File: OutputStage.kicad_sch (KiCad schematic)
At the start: 13 parts, among them SW10 SW_DPDT_x2, SW11 SW_Rotary_1x7, U5 BUF634A

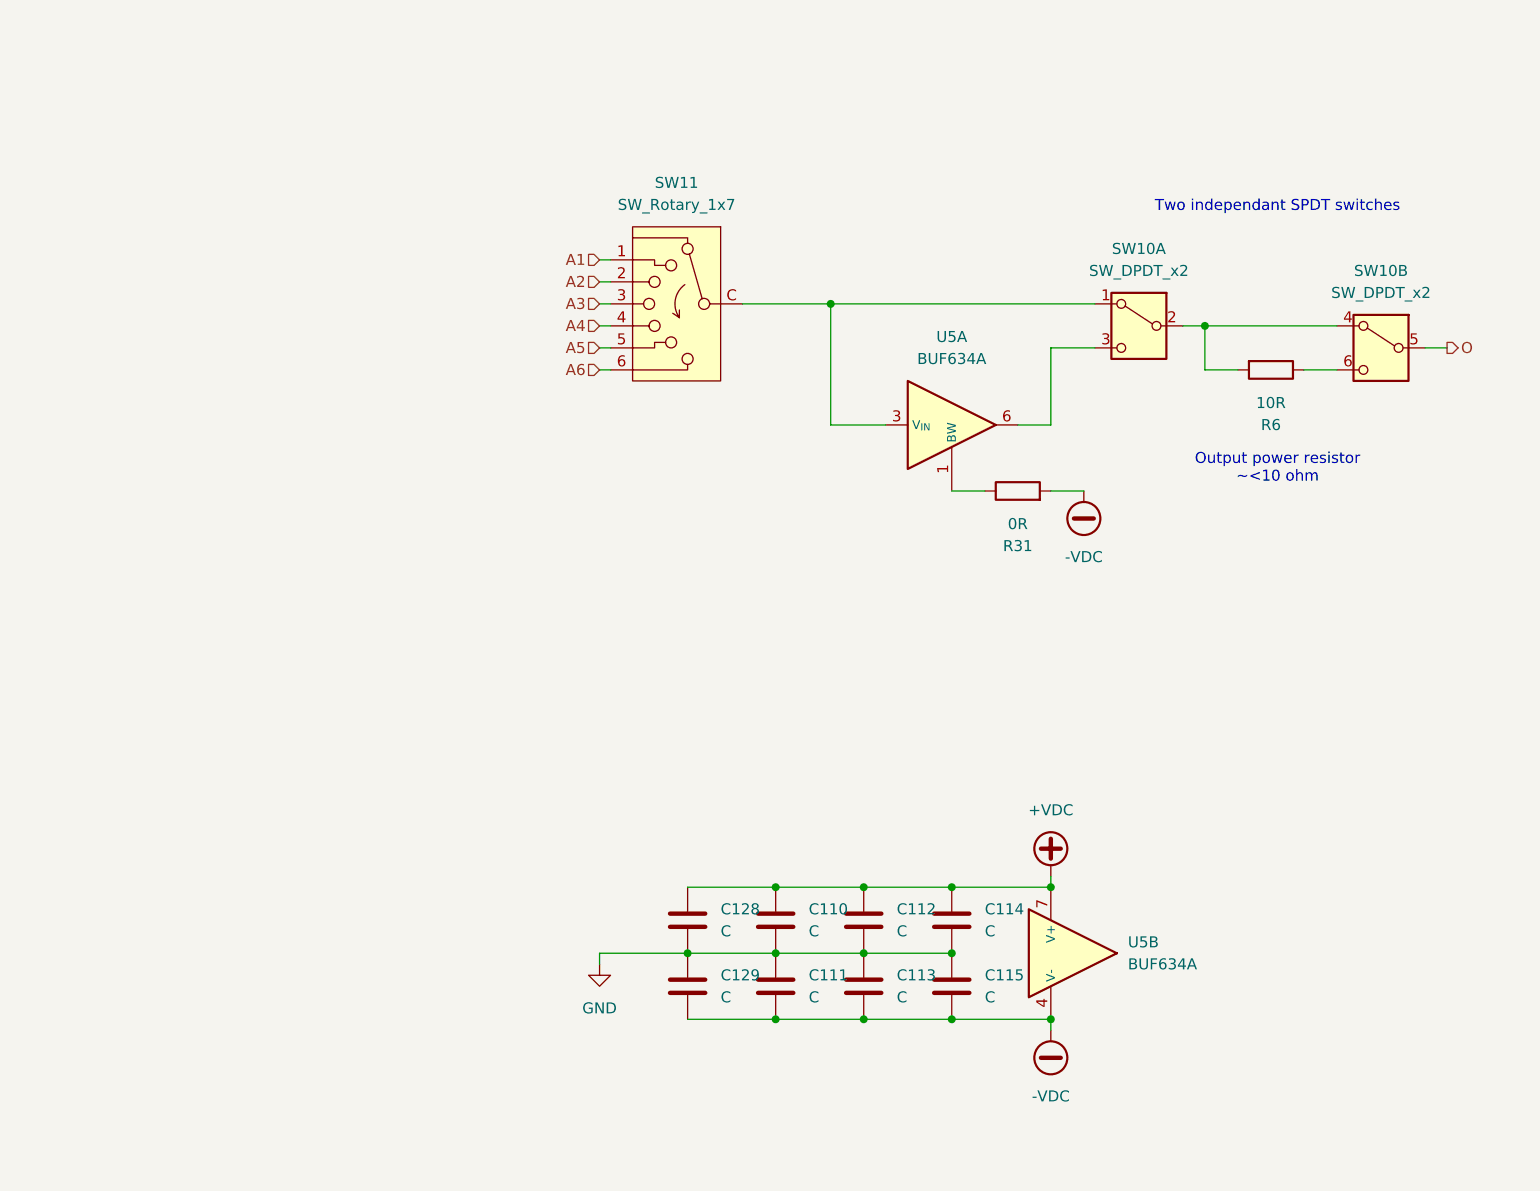
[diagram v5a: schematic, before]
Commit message: Voltage controlled current output circuit and preliminary layout added
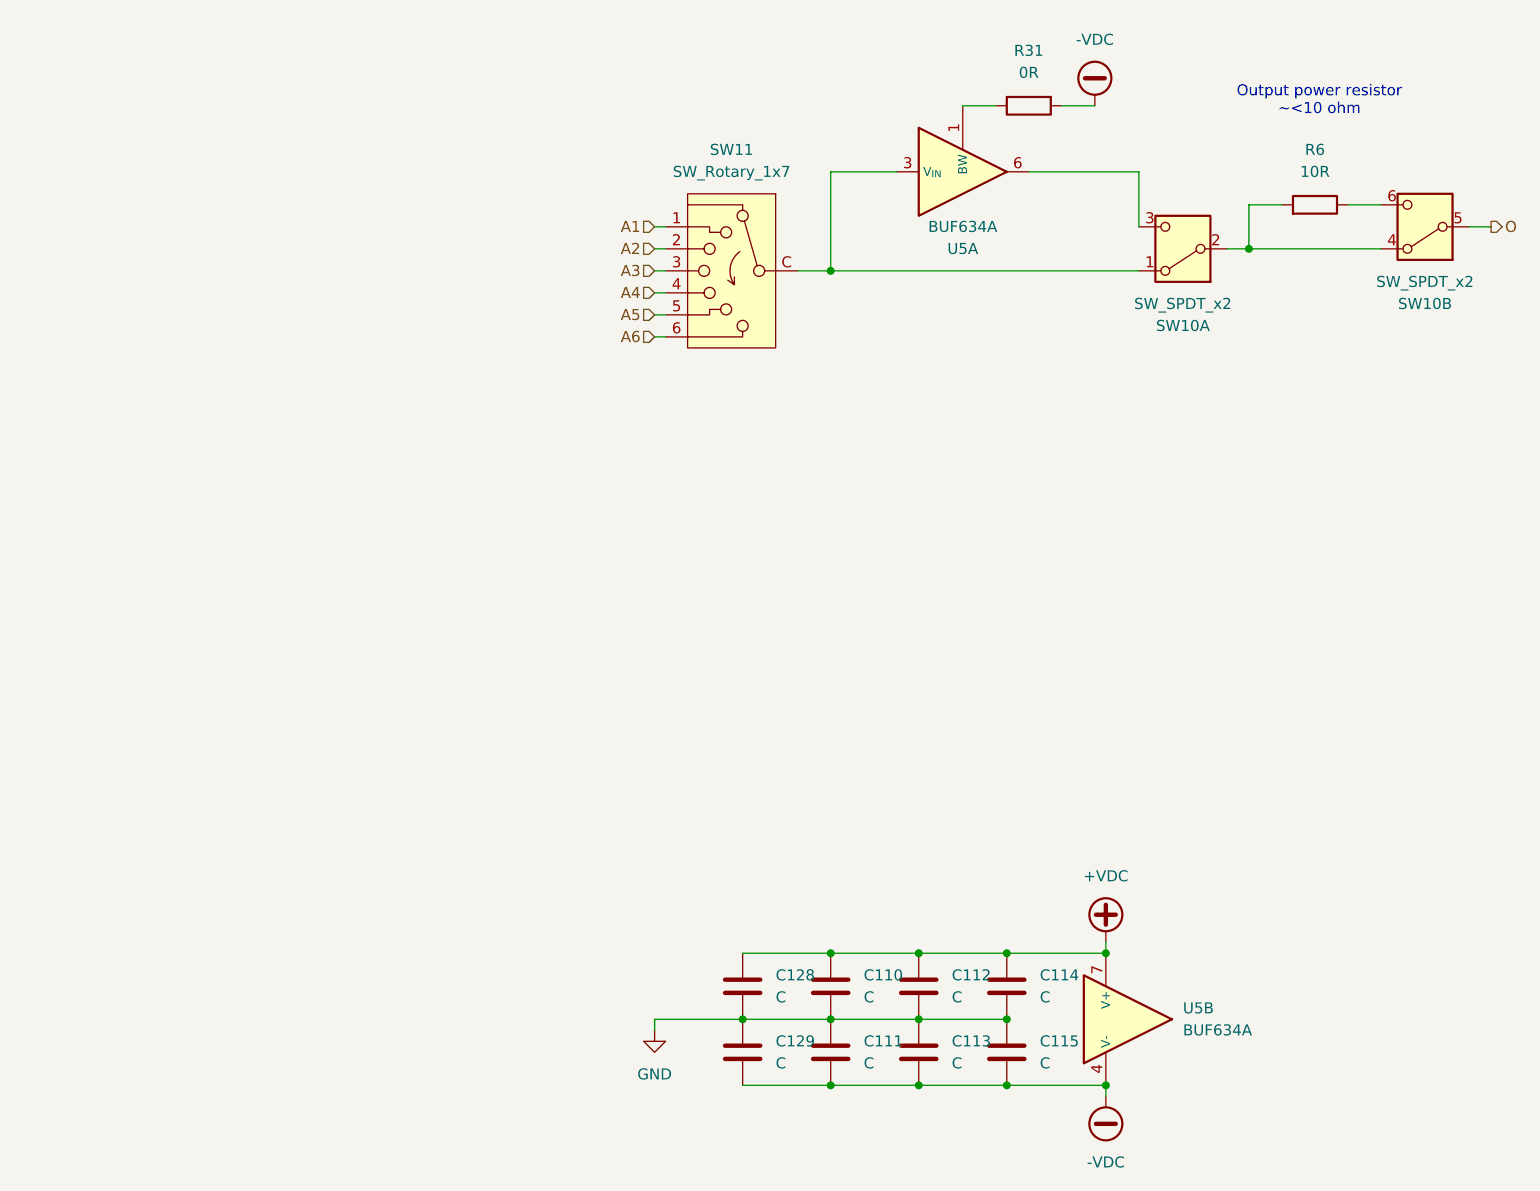
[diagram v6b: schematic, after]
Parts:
- SW10: value SW_DPDT_x2 -> SW_SPDT_x2
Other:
- note removed: "Two independant SPDT switches"
- moved on the sheet: C110, C111, C112, C113, C114, C115, C128, C129, R31, R6, SW10A, SW10B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
